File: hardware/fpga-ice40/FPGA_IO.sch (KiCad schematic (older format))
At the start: 1 part, among them U1 iCE40HX4K-TQ144

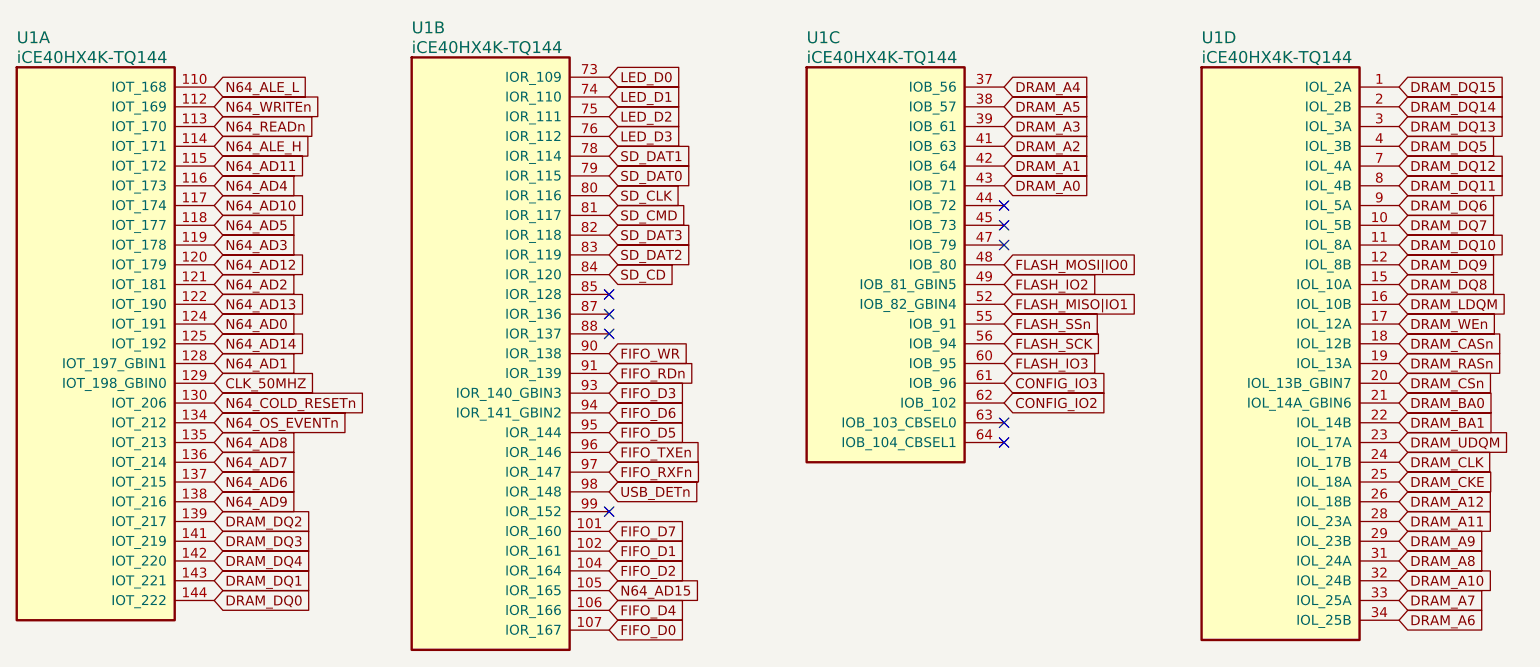
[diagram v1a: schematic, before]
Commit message: Eliminate routing stubs on flash memory
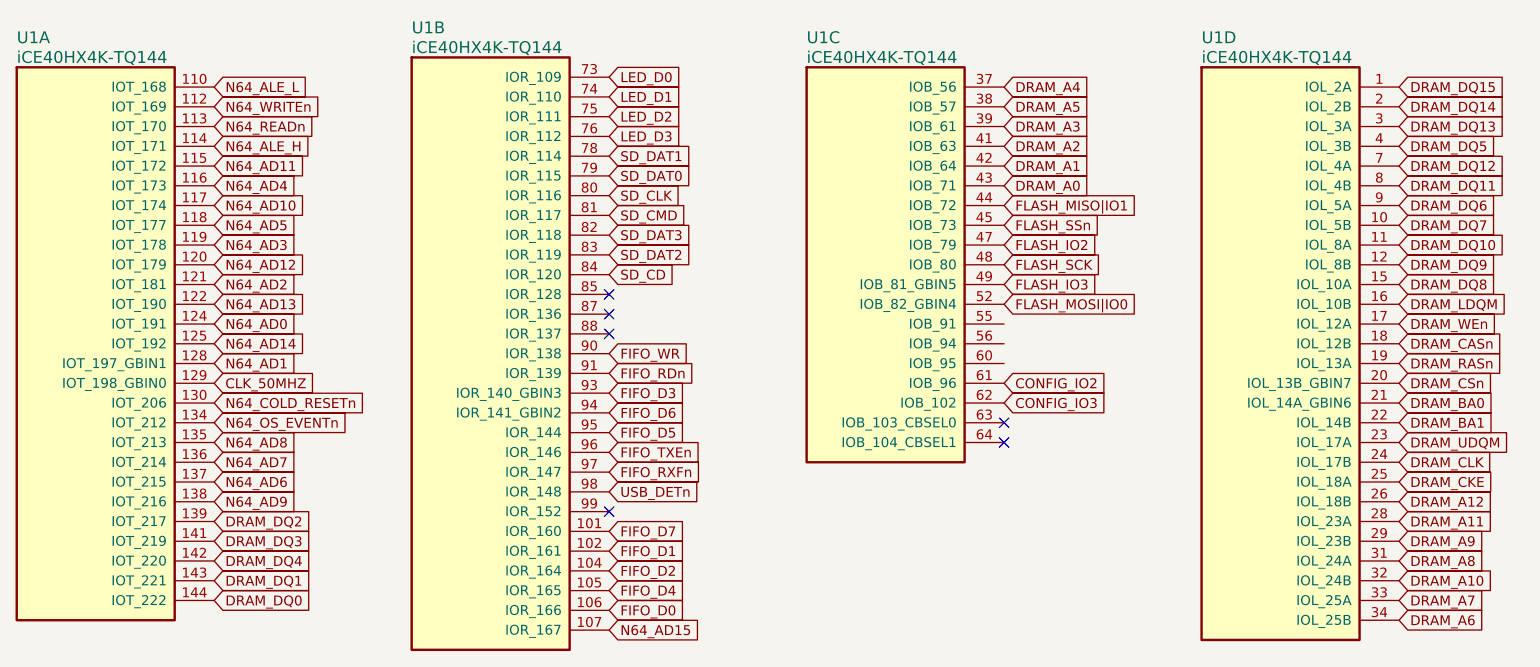
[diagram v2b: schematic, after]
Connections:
- net CONFIG_IO2: now also U1.61 (IOB_96); no longer U1.62 (IOB_102)
- net CONFIG_IO3: now also U1.62 (IOB_102); no longer U1.61 (IOB_96)
- net FIFO_D0: now also U1.106 (IOR_166); no longer U1.107 (IOR_167)
- net FIFO_D4: now also U1.105 (IOR_165); no longer U1.106 (IOR_166)
- net FLASH_IO2: now also U1.47 (IOB_79); no longer U1.49 (IOB_81_GBIN5)
- net FLASH_IO3: now also U1.49 (IOB_81_GBIN5); no longer U1.60 (IOB_95)
- net FLASH_MISO|IO1: now also U1.44 (IOB_72); no longer U1.52 (IOB_82_GBIN4)
- net FLASH_MOSI|IO0: now also U1.52 (IOB_82_GBIN4); no longer U1.48 (IOB_80)
- net FLASH_SCK: now also U1.48 (IOB_80); no longer U1.56 (IOB_94)
- net FLASH_SSn: now also U1.45 (IOB_73); no longer U1.55 (IOB_91)
- net N64_AD15: now also U1.107 (IOR_167); no longer U1.105 (IOR_165)
- no-connect marks 9 -> 6
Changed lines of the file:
@@
 Comment4 ""
 $EndDescr
-NoConn ~ 6850 3650
-NoConn ~ 6850 3550
-NoConn ~ 6850 3450
 NoConn ~ 4850 4100
 NoConn ~ 4850 4000
@@
 Text GLabel 4850 4500 2    50   Input ~ 0
 FIFO_D6
-Text GLabel 4850 5500 2    50   Input ~ 0
+Text GLabel 4850 5400 2    50   Input ~ 0
 FIFO_D4
 Text GLabel 4850 4400 2    50   Input ~ 0
@@
 Text GLabel 4850 5200 2    50   Input ~ 0
 FIFO_D1
-Text GLabel 4850 5600 2    50   Input ~ 0
+Text GLabel 4850 5500 2    50   Input ~ 0
 FIFO_D0
 Text GLabel 6850 2950 2    50   Input ~ 0
@@
 Text GLabel 2850 3850 2    50   Input ~ 0
 N64_AD2
-Text GLabel 4850 5400 2    50   Input ~ 0
+Text GLabel 4850 5600 2    50   Input ~ 0
 N64_AD15
 Text GLabel 2850 4050 2    50   Input ~ 0
 N64_AD0
-Text GLabel 6850 4250 2    50   Input ~ 0
+Text GLabel 6850 3850 2    50   Input ~ 0
 FLASH_IO3
-Text GLabel 6850 3850 2    50   Input ~ 0
+Text GLabel 6850 3650 2    50   Input ~ 0
 FLASH_IO2
+Text GLabel 6850 3450 2    50   Input ~ 0
+FLASH_MISO|IO1
 Text GLabel 6850 3950 2    50   Input ~ 0
-FLASH_MISO|IO1
+FLASH_MOSI|IO0
 Text GLabel 6850 3750 2    50   Input ~ 0
-FLASH_MOSI|IO0
-Text GLabel 6850 4150 2    50   Input ~ 0
 FLASH_SCK
-Text GLabel 6850 4050 2    50   Input ~ 0
-FLASH_SSn
 NoConn ~ 6850 4650
 NoConn ~ 6850 4550
+Text GLabel 6850 4450 2    50   Input ~ 0
+CONFIG_IO3
 Text GLabel 6850 4350 2    50   Input ~ 0
-CONFIG_IO3
-Text GLabel 6850 4450 2    50   Input ~ 0
 CONFIG_IO2
 $Comp
@@
 N64_AD1
 NoConn ~ 4850 5000
+Text GLabel 6850 3550 2    50   Input ~ 0
+FLASH_SSn
 $EndSCHEMATC
